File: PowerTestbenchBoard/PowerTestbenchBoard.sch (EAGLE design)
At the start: 2 parts, among them J8 182-037-213R531, J9 182-025-213R531

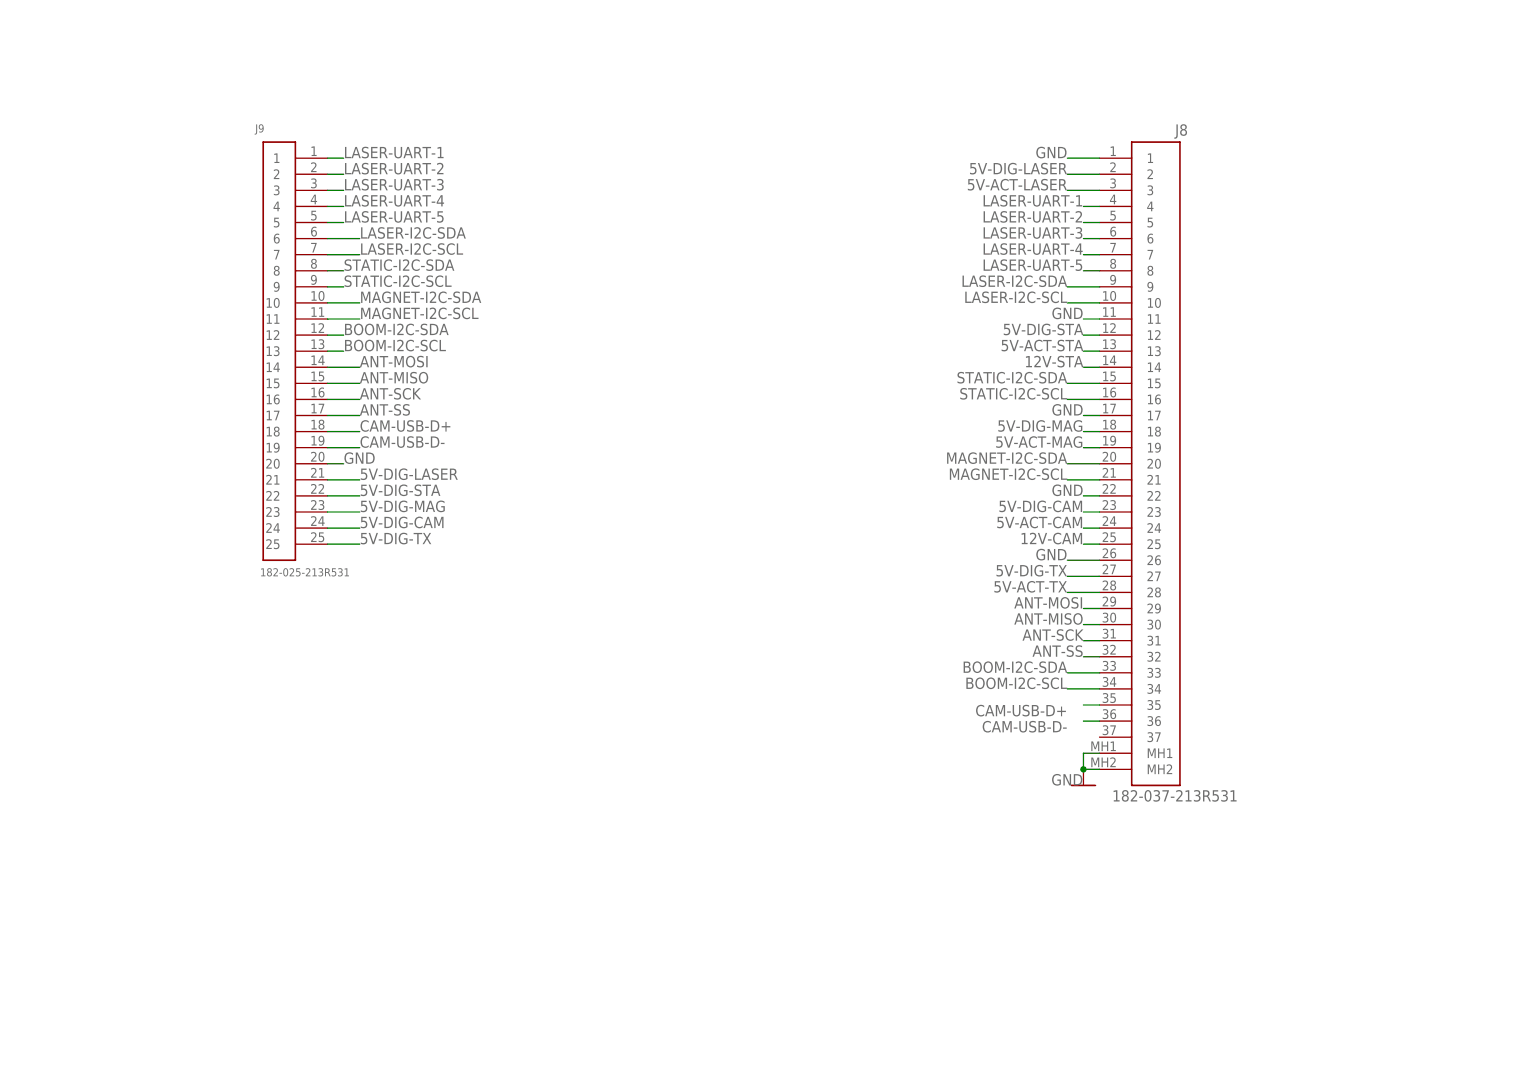
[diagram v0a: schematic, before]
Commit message: Started power test bench schem, mostly done
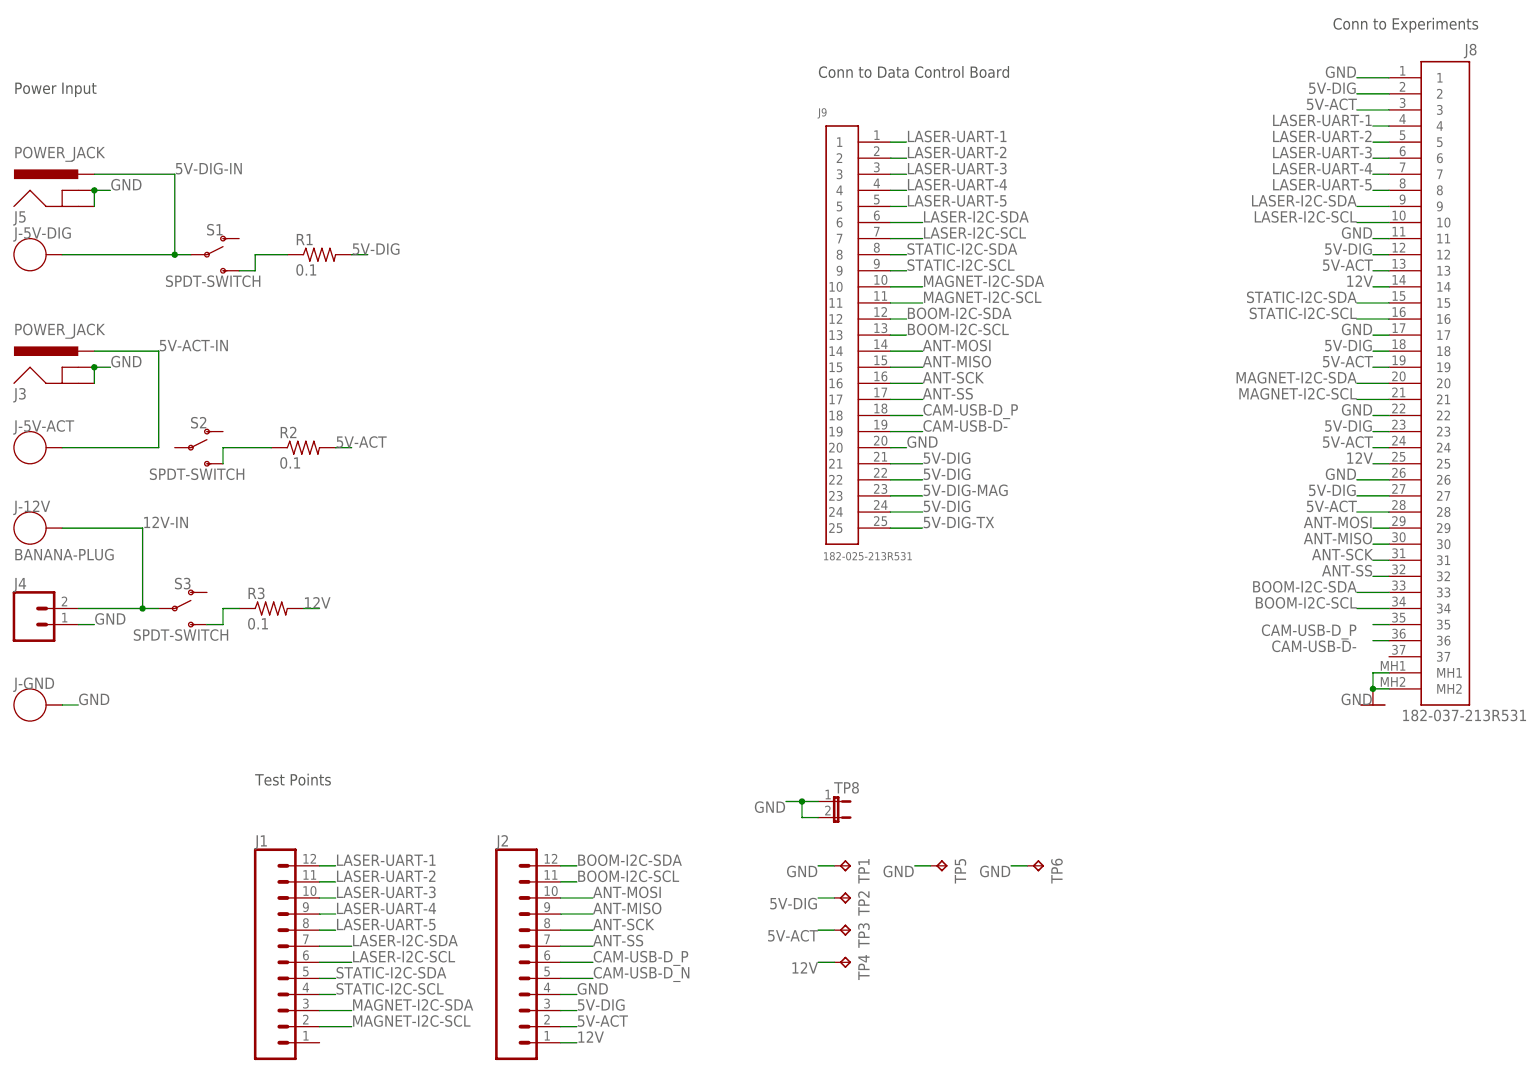
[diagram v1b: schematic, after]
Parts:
- added J-12V, J-5V-ACT, J-5V-DIG, J-GND: BANANA-PLUG, PowerManagementParts:BANANA-PLUG
- added J1, J2: (no value), SparkFun-Connectors:CONN_12
- added J3, J5: POWER_JACK, SparkFun-Connectors:POWER_JACK
- added J4: (no value), SparkFun-Connectors:CONN_023.5MM
- added R1, R2, R3: 0.1, rcl:R-US_R1206
- added S1, S2, S3: SPDT-SWITCH, PowerManagementParts:SPDT-SWITCH
- added TP1, TP2, TP3, TP4, TP5, TP6: TPPAD1-13, testpad:TPPAD1-13
- added TP8: (no value), jumper:JP1E
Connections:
- removed net 12V-CAM: J8.25
- removed net 12V-STA: J8.14
- removed net 5V-ACT-CAM: J8.24
- removed net 5V-ACT-LASER: J8.3
- removed net 5V-ACT-MAG: J8.19
- removed net 5V-ACT-STA: J8.13
- removed net 5V-ACT-TX: J8.28
- removed net 5V-DIG-CAM: J8.23, J9.24
- removed net 5V-DIG-LASER: J8.2, J9.21
- removed net 5V-DIG-STA: J8.12, J9.22
- removed net CAM-USB-D+: J8.35, J9.18
- new net 12V: J2.1, J8.14, J8.25, R3.2, TP4.TP
- new net 12V-IN: J-12V.P$1, J4.2, S3.P
- new net 5V-ACT: J2.2, J8.13, J8.19, J8.24, J8.28, J8.3, R2.2, TP3.TP
- new net 5V-ACT-IN: J-5V-ACT.P$1, J3.PWR
- new net 5V-DIG: J2.3, J8.12, J8.18, J8.2, J8.23, J8.27, J9.21, J9.22, J9.24, R1.2, TP2.TP
- new net 5V-DIG-IN: J-5V-DIG.P$1, J5.PWR, S1.P
- new net CAM-USB-D_N: J2.5
- new net CAM-USB-D_P: J2.6, J8.35, J9.18
- new net N$1: R1.1, S1.S
- new net N$2: R2.1, S2.S
- new net N$3: R3.1, S3.S
- net 5V-DIG-MAG: no longer J8.18
- net 5V-DIG-TX: no longer J8.27
- net ANT-MISO: now also J2.9
- net ANT-MOSI: now also J2.10
- net ANT-SCK: now also J2.8
- net ANT-SS: now also J2.7
- net BOOM-I2C-SCL: now also J2.11
- net BOOM-I2C-SDA: now also J2.12
- net GND: now also J-GND.P$1, J2.4, J3.GND, J3.GNDBREAK, J4.1, J5.GND, J5.GNDBREAK, TP1.TP, TP5.TP, TP6.TP, TP8.1, TP8.2
- net LASER-I2C-SCL: now also J1.6
- net LASER-I2C-SDA: now also J1.7
- net LASER-UART-1: now also J1.12
- net LASER-UART-2: now also J1.11
- net LASER-UART-3: now also J1.10
- net LASER-UART-4: now also J1.9
- net LASER-UART-5: now also J1.8
- net MAGNET-I2C-SCL: now also J1.2
- net MAGNET-I2C-SDA: now also J1.3
- net STATIC-I2C-SCL: now also J1.4
- net STATIC-I2C-SDA: now also J1.5
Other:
- note added: "Conn to Data Control Board"
- note added: "Conn to Experiments"
- note added: "Power Input"
- note added: "Test Points"
- moved on the sheet: J8, J9

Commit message: Board mostly routed. Added indicator LEDs and protection diodes
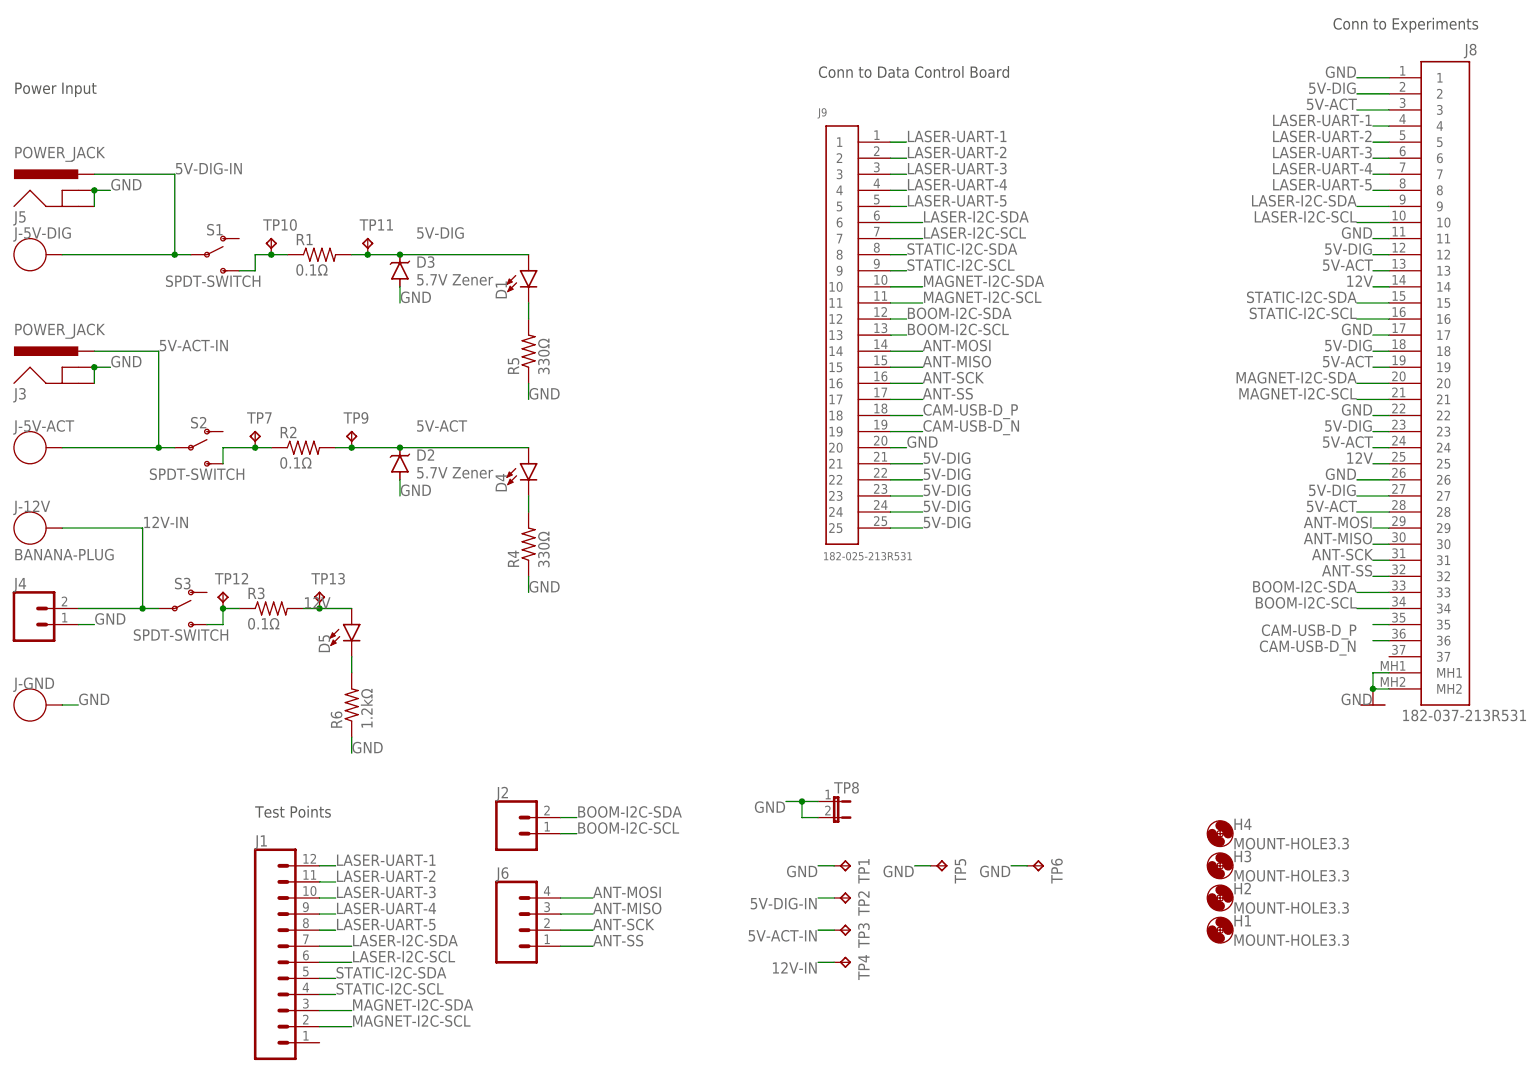
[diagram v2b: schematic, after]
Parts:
- added D1, D4, D5: (no value), SparkFun-LED:LED-3MM-NO_SILK
- added D2, D3: 5.7V Zener, PowerManagementParts:ZENER-GENERICSMB
- added H1, H2, H3, H4: MOUNT-HOLE3.3, holes:MOUNT-HOLE3.3
- added J6: (no value), SparkFun-Connectors:CONN_04
- added R4, R5: 330Ω, rcl:R-US_R0805
- added R6: 1.2kΩ, rcl:R-US_R0805
- added TP10, TP11, TP12, TP13, TP7, TP9: TPPAD1-13, testpad:TPPAD1-13
- J2: device SparkFun-Connectors:CONN_12 -> SparkFun-Connectors:CONN_02
- R1, R2, R3: value 0.1 -> 0.1Ω
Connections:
- removed net 5V-DIG-MAG: J9.23
- removed net 5V-DIG-TX: J9.25
- removed net CAM-USB-D-: J8.36, J9.19
- new net N$4: D4.C, R4.2
- new net N$5: D5.C, R6.2
- new net N$6: D1.C, R5.2
- net 12V: now also D5.A, TP13.TP; no longer J2.1, TP4.TP
- net 12V-IN: now also TP4.TP
- net 5V-ACT: now also D2.C, D4.A, TP9.TP; no longer J2.2, TP3.TP
- net 5V-ACT-IN: now also S2.P, TP3.TP
- net 5V-DIG: now also D1.A, D3.C, J9.23, J9.25, TP11.TP; no longer J2.3, TP2.TP
- net 5V-DIG-IN: now also TP2.TP
- net ANT-MISO: now also J6.3; no longer J2.9
- net ANT-MOSI: now also J6.4; no longer J2.10
- net ANT-SCK: now also J6.2; no longer J2.8
- net ANT-SS: now also J6.1; no longer J2.7
- net BOOM-I2C-SCL: now also J2.1; no longer J2.11
- net BOOM-I2C-SDA: now also J2.2; no longer J2.12
- net CAM-USB-D_N: now also J8.36, J9.19; no longer J2.5
- net CAM-USB-D_P: no longer J2.6
- net GND: now also D2.A, D3.A, R4.1, R5.1, R6.1; no longer J2.4
- net N$1: now also TP10.TP
- net N$2: now also TP7.TP
- net N$3: now also TP12.TP

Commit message: Ready to manufacture
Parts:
- removed TP6: TPPAD1-13, testpad:TPPAD1-13
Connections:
- net GND: now also J1.1; no longer TP6.TP
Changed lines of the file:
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@@
 <part name="TP8" library="jumper" library_urn="urn:adsk.eagle:library:252" deviceset="JP1E" device="" package3d_urn="urn:adsk.eagle:package:15455/1"/>
 <part name="TP5" library="testpad" library_urn="urn:adsk.eagle:library:385" deviceset="TP" device="PAD1-13" package3d_urn="urn:adsk.eagle:package:27946/1"/>
-<part name="TP6" library="testpad" library_urn="urn:adsk.eagle:library:385" deviceset="TP" device="PAD1-13" package3d_urn="urn:adsk.eagle:package:27946/1"/>
 <part name="S1" library="PowerManagementParts" deviceset="SPDT-SWITCH" device=""/>
 <part name="S2" library="PowerManagementParts" deviceset="SPDT-SWITCH" device=""/>
@@
 <attribute name="TP_SIGNAL_NAME" x="161.29" y="39.37" size="1.778" layer="97" rot="R270"/>
 </instance>
-<instance part="TP6" gate="G$1" x="177.8" y="40.64" smashed="yes" rot="R270">
-<attribute name="NAME" x="179.07" y="41.91" size="1.778" layer="95" rot="R270"/>
-<attribute name="TP_SIGNAL_NAME" x="176.53" y="39.37" size="1.778" layer="97" rot="R270"/>
-</instance>
 <instance part="S1" gate="G$1" x="45.72" y="137.16" smashed="yes">
 <attribute name="NAME" x="46.99" y="140.208" size="1.778" layer="95" font="vector" align="bottom-center"/>
@@
 </segment>
 <segment>
-<pinref part="TP6" gate="G$1" pin="TP"/>
-<wire x1="175.26" y1="40.64" x2="172.72" y2="40.64" width="0.1524" layer="91"/>
-<label x="172.72" y="40.64" size="1.778" layer="95" rot="R180"/>
-</segment>
-<segment>
 <pinref part="D2" gate="G$1" pin="A"/>
 <wire x1="76.2" y1="101.6" x2="76.2" y2="99.06" width="0.1524" layer="91"/>
@@
 <label x="68.58" y="58.42" size="1.778" layer="95"/>
 </segment>
+<segment>
+<pinref part="J1" gate="G$1" pin="1"/>
+<wire x1="63.5" y1="12.7" x2="66.04" y2="12.7" width="0.1524" layer="91"/>
+<label x="66.04" y="12.7" size="1.778" layer="95"/>
+</segment>
 </net>
